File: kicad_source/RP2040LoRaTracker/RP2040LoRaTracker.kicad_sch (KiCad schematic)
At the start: 0 parts

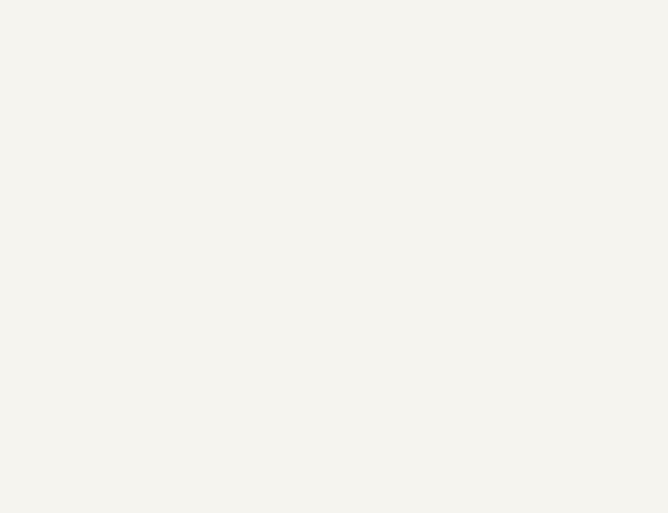
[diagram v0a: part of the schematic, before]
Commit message: beautified layout, made DRC
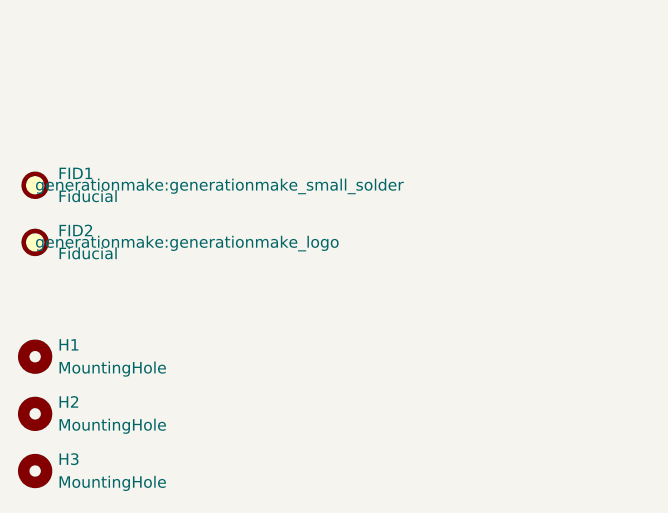
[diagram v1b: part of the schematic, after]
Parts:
- added FID1: Fiducial, generationmake:generationmake_small_solder, symbol Mechanical:Fiducial
- added FID2: Fiducial, generationmake:generationmake_logo, symbol Mechanical:Fiducial
- added H1, H2, H3: MountingHole, MountingHole:MountingHole_2.2mm_M2, symbol Mechanical:MountingHole
